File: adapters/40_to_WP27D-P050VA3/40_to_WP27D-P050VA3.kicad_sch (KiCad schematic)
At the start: 3 parts, among them CN1 WP27D-S050VA3-R15000, J1 Conn_01x05_Pin, U1 ED078KH6

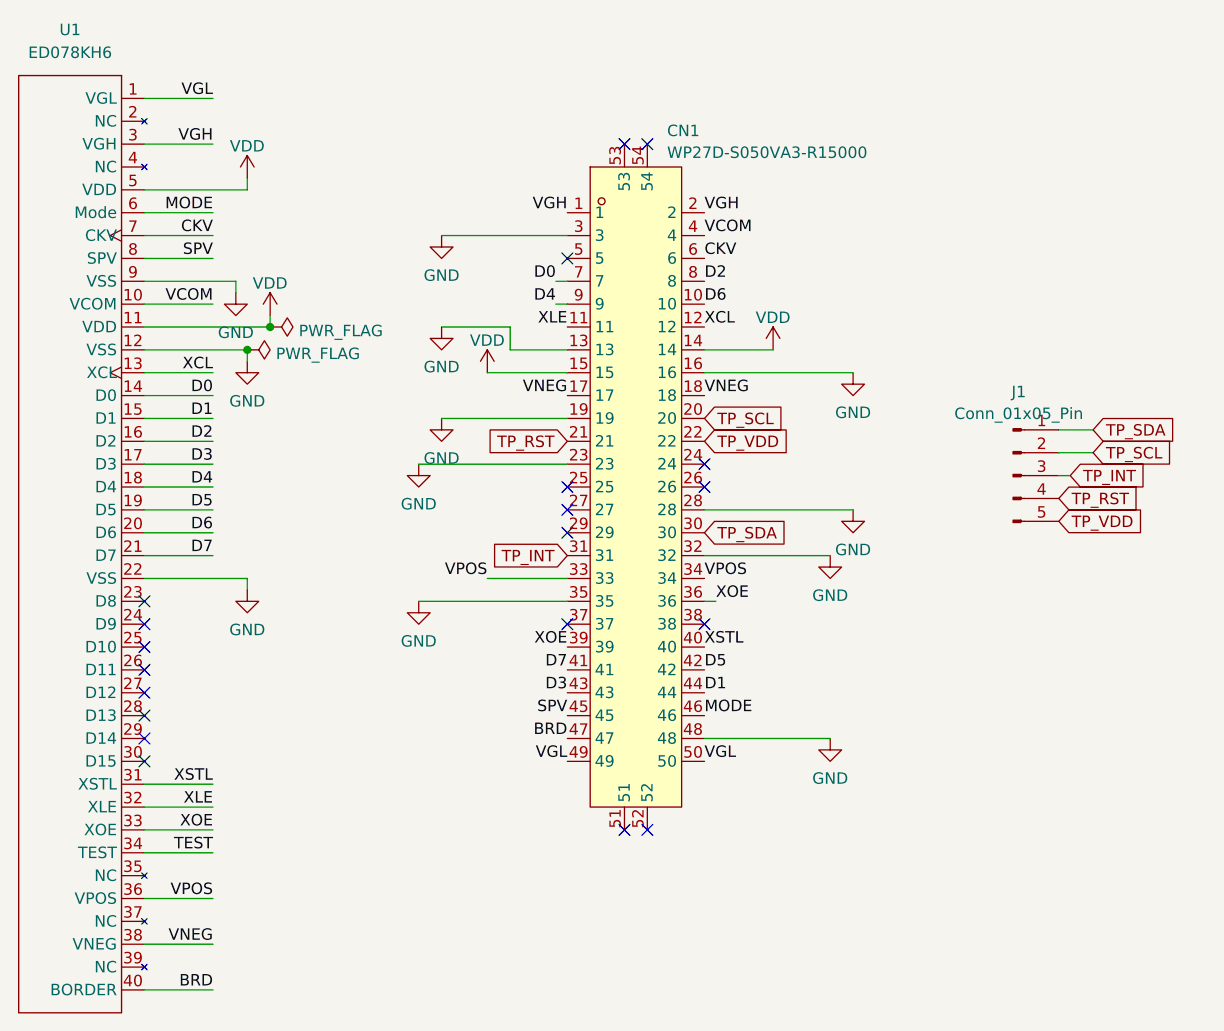
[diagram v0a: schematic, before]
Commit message: Fix adapter with correct pinout
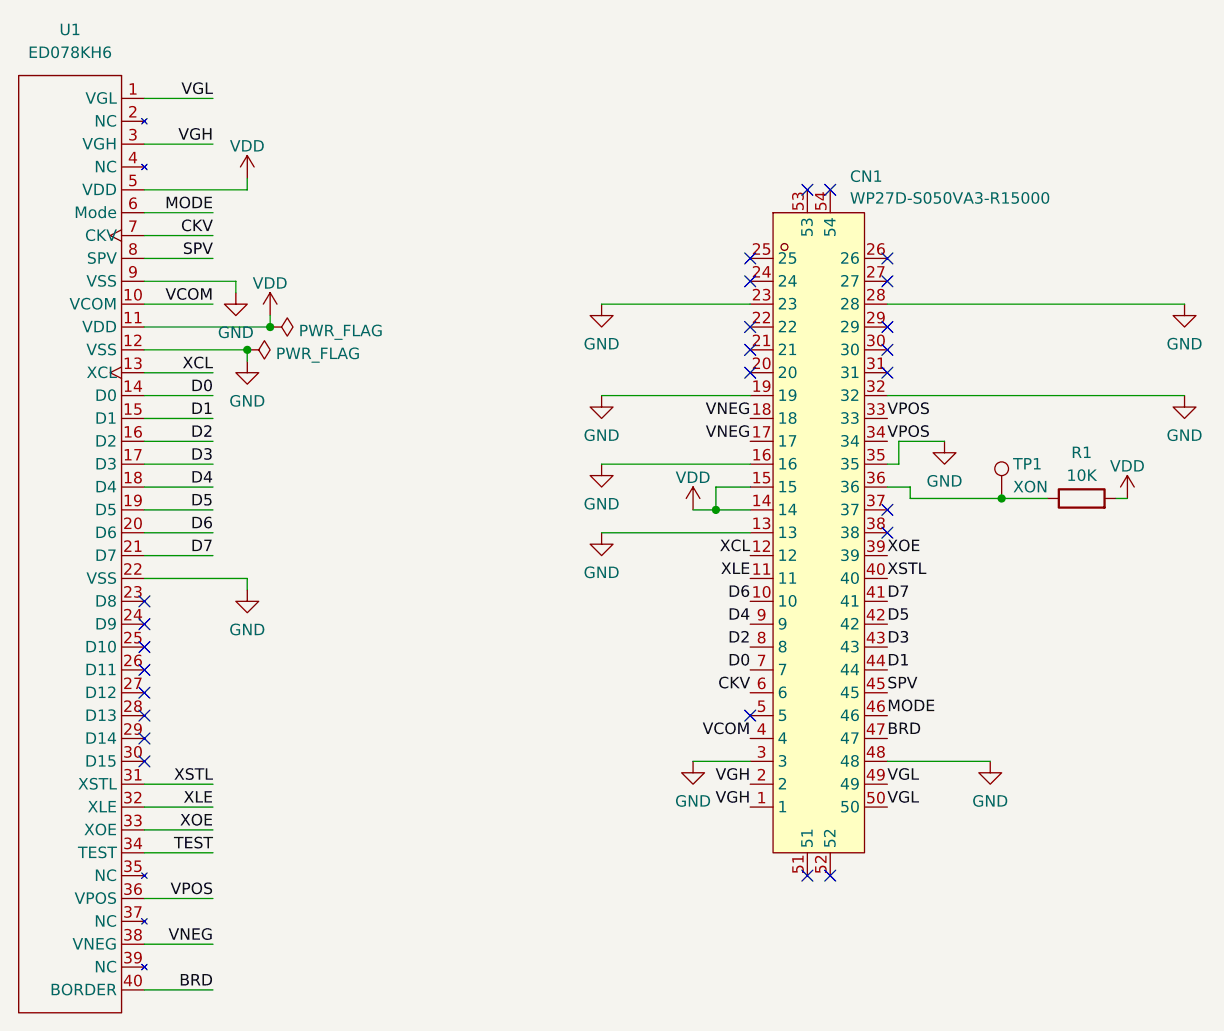
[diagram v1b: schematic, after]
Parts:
- removed J1: Conn_01x05_Pin, Connector_PinHeader_2.54mm:PinHeader_1x05_P2.54mm_Vertical, symbol Connector:Conn_01x05_Pin
- added R1: 10K, Resistor_SMD:R_0603_1608Metric, symbol Device:R
- added TP1: XON, TestPoint:TestPoint_Pad_1.0x1.0mm, symbol Connector:TestPoint
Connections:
- net VDD: now also R1.2
- net XOE: no longer CN1.36
- net TP_INT: no longer names the net of CN1.31
- net TP_RST: no longer names the net of CN1.21
- net TP_SCL: no longer names the net of CN1.20
- net TP_SDA: no longer names the net of CN1.30
- net TP_VDD: no longer names the net of CN1.22
- new net: CN1.36, R1.1, TP1.1
- no-connect marks 20 -> 25

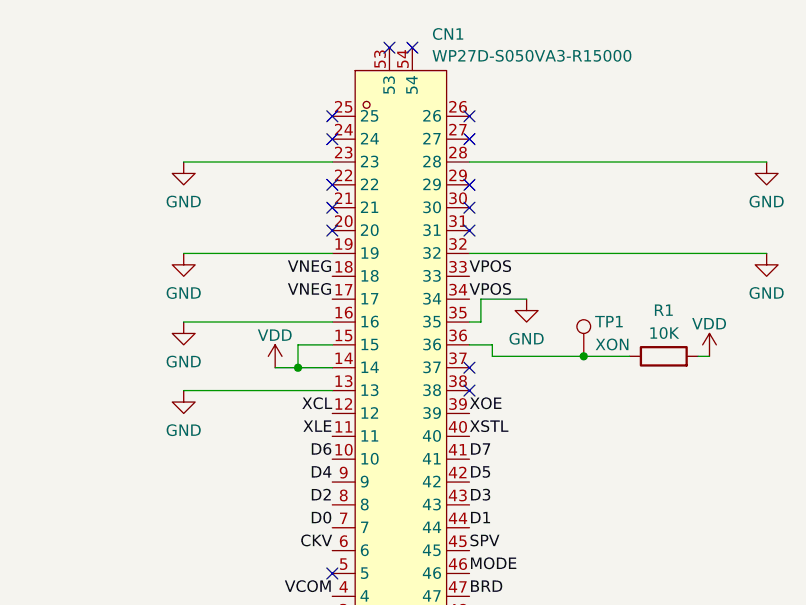
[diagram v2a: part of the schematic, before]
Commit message: Add signals test header
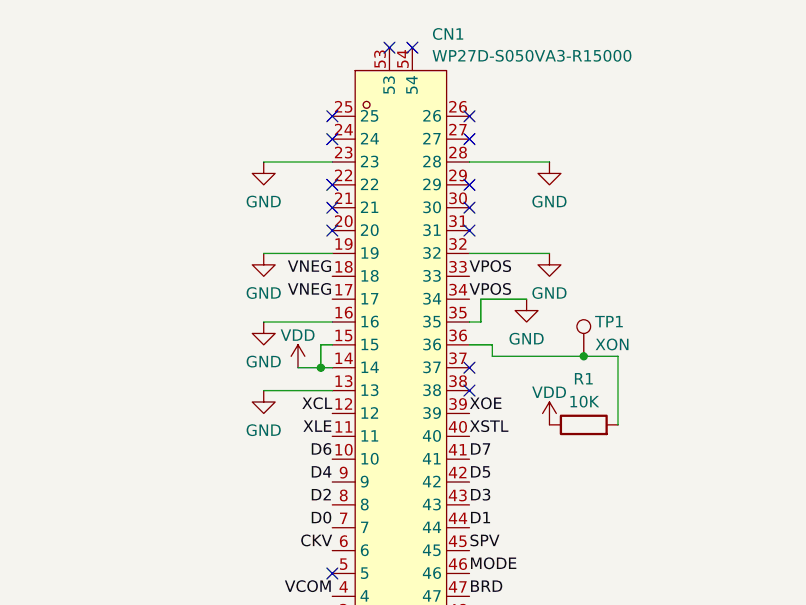
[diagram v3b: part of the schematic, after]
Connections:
- net VDD: now also R1.1; no longer R1.2
- net at CN1.36, TP1.1: now also R1.2; no longer R1.1
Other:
- moved on the sheet: R1
